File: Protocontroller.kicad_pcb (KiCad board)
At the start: 4 copper layers, 51 x 26.4 mm, 39 parts, among them U1 AP2112K-3.3TRG1, U2 PM254-1-14-Z-8.5, U3 PM254-1-14-Z-8.5, U4 SN74AHCT245PWR, U5 SN74AHCT245PWR, U6 SN74AHCT374PWR, U8 HC-JN254-2-08-W

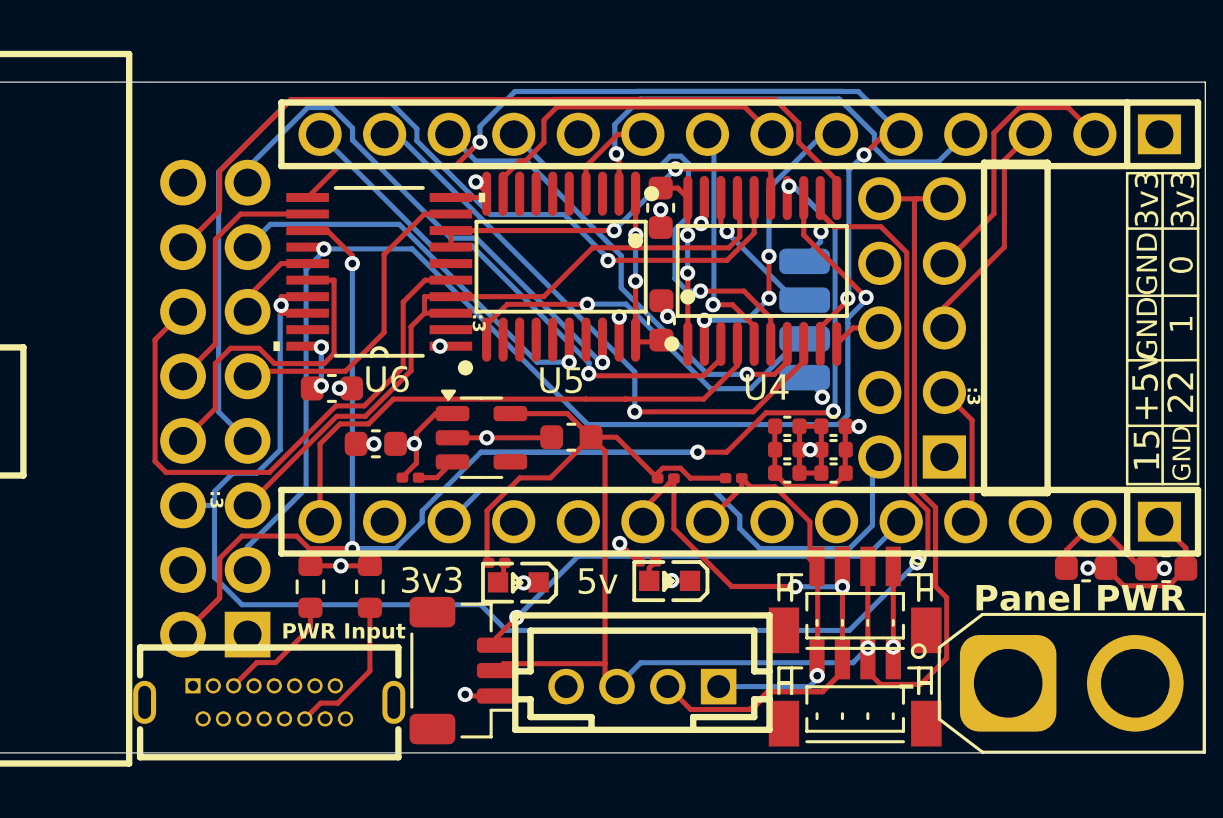
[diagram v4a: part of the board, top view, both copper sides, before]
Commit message: Switch Pullups to use 4.7k Resistors for improved speeds, Adjusted capacitors, removed Designators file
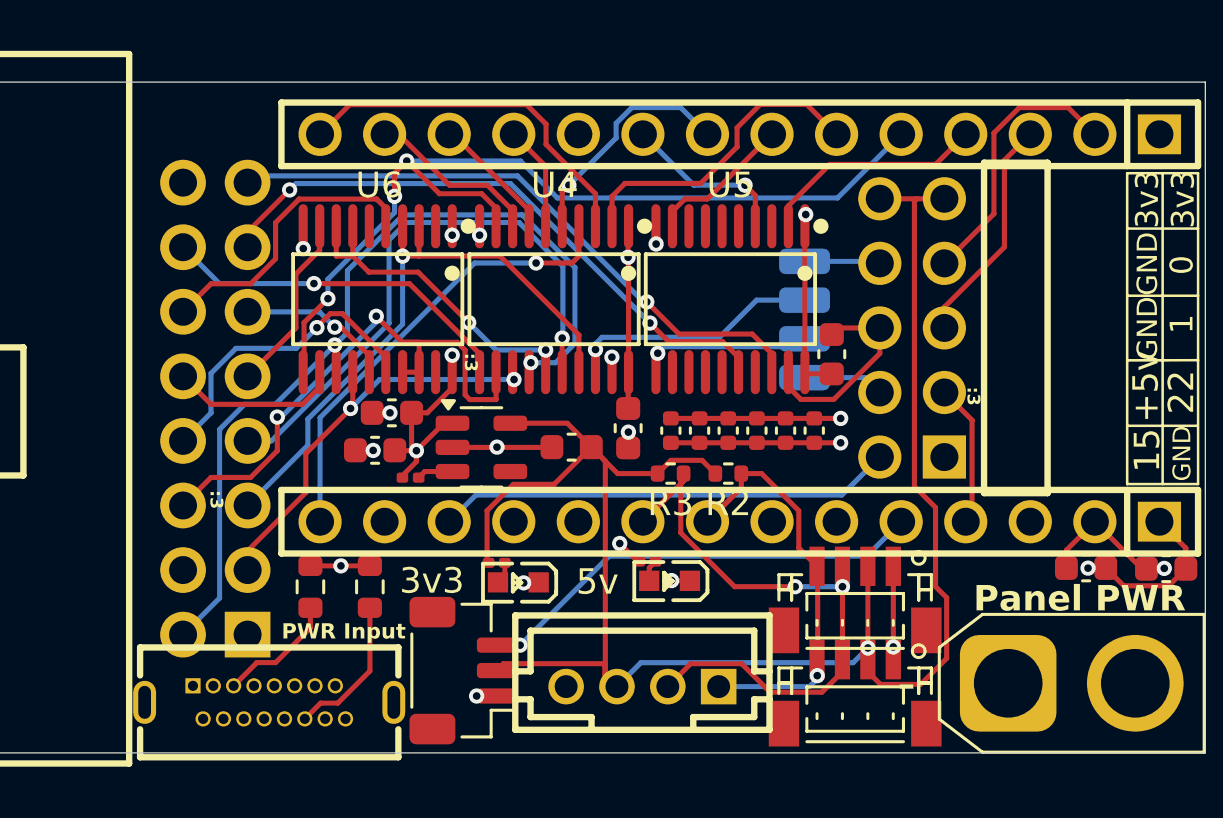
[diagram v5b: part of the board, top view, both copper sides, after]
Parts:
- R2, R3: value 10K_0201 -> 4.7K_0402; footprint Resistor_SMD:R_0201_0603Metric -> Resistor_SMD:R_0402_1005Metric
- moved C6 8.76 mm to (116.3, 126.1)
- moved U4 8.27 mm to (113.3, 121.0), turned to 180 degrees
- moved C5 6.83 mm to (124.3, 123.2)
- moved U5 6.78 mm to (120.3, 121.0)
- moved C8 6.61 mm to (117.9, 126.2), turned to -90 degrees
- moved C9 3.83 mm to (119.1, 126.2), turned to -90 degrees
- moved C7 2.55 mm to (107.0, 125.5), turned to 0 degrees
- moved C10 2.44 mm to (120.2, 126.2), turned to -90 degrees
- moved C12 2.03 mm to (122.5, 126.2), turned to -90 degrees
- moved C11 1.21 mm to (121.3, 126.2), turned to -90 degrees
- moved U6 1.08 mm to (106.4, 121.0)
- moved C13 0.78 mm to (123.6, 126.2), turned to -90 degrees
- moved C2 0.39 mm to (114.0, 126.9)
- moved U1 0.38 mm to (110.5, 126.9)
- moved R2 0.28 mm to (120.2, 127.9)
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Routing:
- net /PANEL_G2: track 64.9 -> 22.5 mm
- net /PANEL_G1: track 69.3 -> 34.9 mm, vias 5 -> 2
- net /PANEL_B1: track 48.0 -> 16.7 mm
- net /PANEL_LATCH: track 31.5 -> 14.1 mm, vias 0 -> 1
- net /BUFFER_G2/MOSI: track 23.9 -> 6.90 mm, vias 1 -> 0
- net /PANEL_B2: track 38.1 -> 22.8 mm
- net /BUFFER_B1: track 19.0 -> 5.01 mm, vias 1 -> 0
- net /BUFFER_G1: track 17.9 -> 4.14 mm, vias 1 -> 0
- net /PANEL_ADX3: track 22.8 -> 11.5 mm
- net /BUFFER_OE: track 18.8 -> 8.95 mm, vias 1 -> 0
- net /APA_DAT: track 15.6 -> 6.78 mm
- net /PANEL_CLK: track 16.2 -> 24.1 mm, vias 1 -> 2
- net /FLEXIO_MOSI: track 13.3 -> 5.75 mm
- net GND: track 45.7 -> 52.2 mm, vias 17 -> 16
- net /BUFFER_R2: track 20.8 -> 14.5 mm, vias 1 -> 0
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
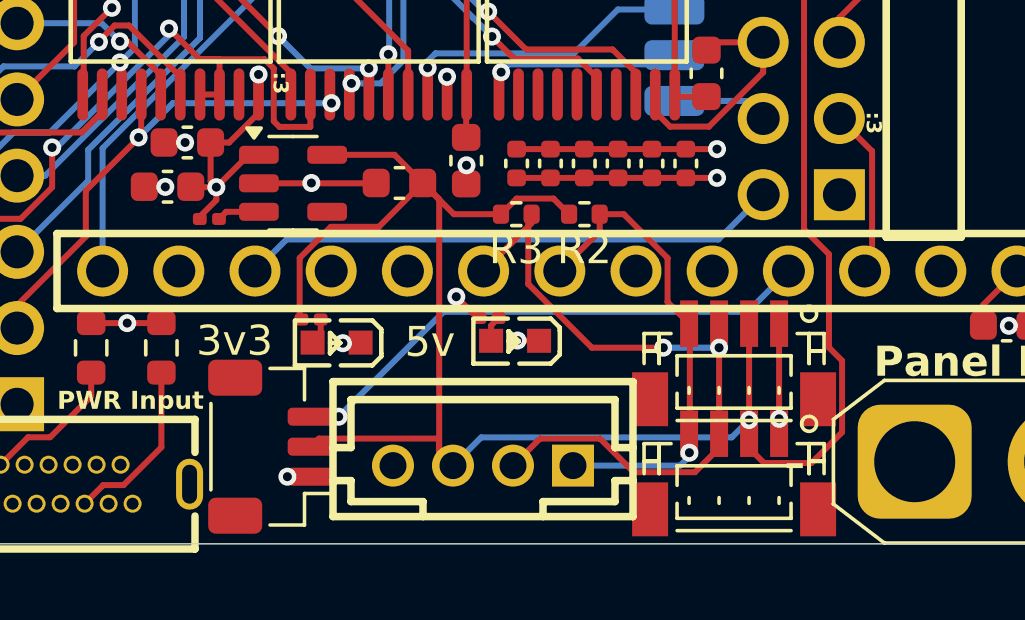
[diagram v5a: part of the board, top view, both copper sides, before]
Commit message: Removed 0201 Resistors for Compatablity with Economic PCBA's, moved JST SH ports so I2C-1 Pins dont phase through teensy headers
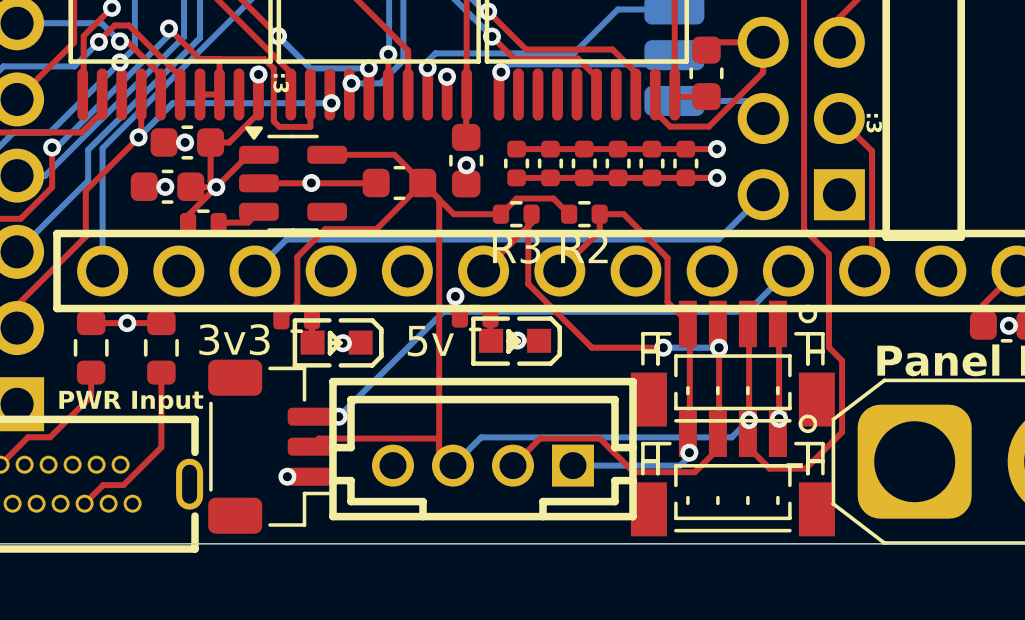
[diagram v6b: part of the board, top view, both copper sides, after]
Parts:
- R1, R4, R5: footprint Resistor_SMD:R_0201_0603Metric -> Resistor_SMD:R_0402_1005Metric
- moved R4 0.48 mm to (110.6, 131.4)
- moved R5 0.46 mm to (116.6, 131.4)
- moved R1 0.23 mm to (107.5, 128.2)

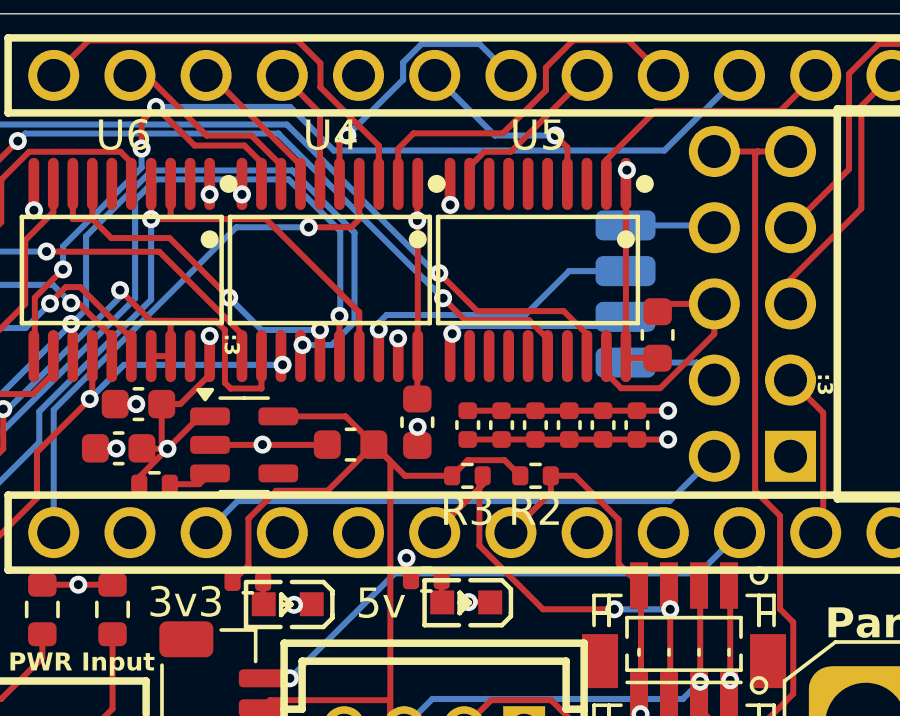
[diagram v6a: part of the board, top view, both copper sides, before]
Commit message: Fix Compat with Economic Again
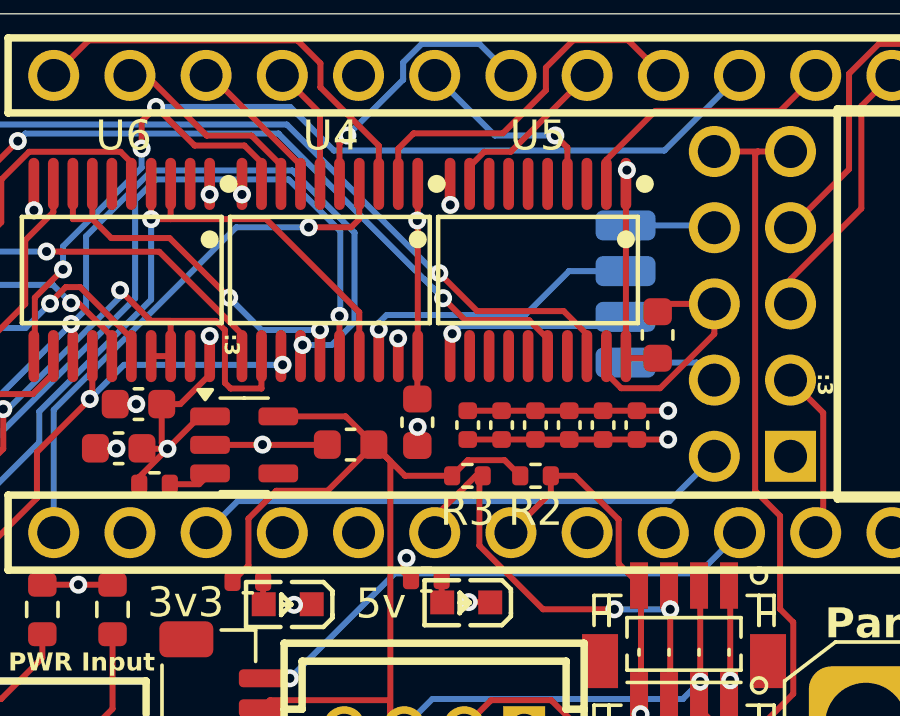
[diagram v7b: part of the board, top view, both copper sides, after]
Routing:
- net +5V: track 54.6 -> 53.9 mm
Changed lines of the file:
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@@
-	)
-	(segment
-		(start 116.258 119.39)
-		(end 116.258 118.765)
-		(width 0.2)
-		(layer "F.Cu")
-		(net 1)
 	)
 	(segment
@@
 	)
 	(segment
+		(start 116.275 119.373)
+		(end 116.258 119.39)
+		(width 0.2)
+		(layer "F.Cu")
+		(net 1)
+	)
+	(segment
 		(start 109.3375 123.91)
 		(end 109.3375 124.5325)
@@
 	)
 	(segment
-		(start 116.258 118.765)
-		(end 116.275 118.748)
-		(width 0.2)
-		(layer "F.Cu")
-		(net 1)
-	)
-	(segment
 		(start 138.2 131.64)
 		(end 137.524 132.316)
@@
 	)
 	(segment
+		(start 116.275 118.17)
+		(end 116.275 119.373)
+		(width 0.2)
+		(layer "F.Cu")
+		(net 1)
+	)
+	(segment
 		(start 107.74 125.51)
 		(end 107.74 126.809)
@@
 	)
 	(segment
-		(start 116.258 118.765)
-		(end 116.258 118.14)
-		(width 0.2)
-		(layer "F.Cu")
-		(net 1)
-	)
-	(segment
 		(start 115.79 130.75)
 		(end 115.79 131.1)
@@
 	)
 	(segment
-		(start 116.275 118.748)
-		(end 116.275 118.17)
-		(width 0.2)
-		(layer "F.Cu")
-		(net 1)
-	)
-	(segment
 		(start 123.212 117.9965)
 		(end 123.212 117.743)
@@
 	)
 	(segment
+		(start 118.21 127.9)
+		(end 118.44 127.9)
+		(width 0.2)
+		(layer "F.Cu")
+		(net 14)
+	)
+	(segment
+		(start 118.329 128.011)
+		(end 118.329 130.229339)
+		(width 0.2)
+		(layer "F.Cu")
+		(net 14)
+	)
+	(segment
+		(start 117.689 128.421)
+		(end 117.697918 128.421)
+		(width 0.2)
+		(layer "F.Cu")
+		(net 14)
+	)
+	(segment
 		(start 121.842 136.5)
 		(end 120.721 135.379)
@@
 	)
 	(segment
+		(start 124.69 132.35)
+		(end 124.69 135.2175)
+		(width 0.2)
+		(layer "F.Cu")
+		(net 14)
+	)
+	(segment
+		(start 117.891 128.227918)
+		(end 117.891 128.219)
+		(width 0.2)
+		(layer "F.Cu")
+		(net 14)
+	)
+	(segment
+		(start 124.69 135.2175)
+		(end 124.69 135.6945)
+		(width 0.2)
+		(layer "F.Cu")
+		(net 14)
+	)
+	(segment
+		(start 116.84 129.794)
+		(end 116.84 129.27)
+		(width 0.2)
+		(layer "F.Cu")
+		(net 14)
+	)
+	(segment
+		(start 118.44 127.9)
+		(end 118.329 128.011)
+		(width 0.2)
+		(layer "F.Cu")
+		(net 14)
+	)
+	(segment
+		(start 118.721 135.379)
+		(end 117.82 136.28)
+		(width 0.2)
+		(layer "F.Cu")
+		(net 14)
+	)
+	(segment
+		(start 118.329 130.229339)
+		(end 120.449661 132.35)
+		(width 0.2)
+		(layer "F.Cu")
+		(net 14)
+	)
+	(segment
+		(start 117.891 128.219)
+		(end 118.21 127.9)
+		(width 0.2)
+		(layer "F.Cu")
+		(net 14)
+	)
+	(segment
+		(start 120.721 135.379)
+		(end 118.721 135.379)
+		(width 0.2)
+		(layer "F.Cu")
+		(net 14)
+	)
+	(segment
+		(start 123.8845 136.5)
+		(end 121.842 136.5)
+		(width 0.2)
+		(layer "F.Cu")
+		(net 14)
+	)
+	(segment
+		(start 124.69 131.548)
+		(end 124.69 132.35)
+		(width 0.2)
+		(layer "F.Cu")
+		(net 14)
+	)
+	(segment
 		(start 120.449661 132.35)
 		(end 122.83 132.35)
@@
 	)
 	(segment
-		(start 124.69 132.35)
-		(end 124.69 135.2175)
-		(width 0.2)
-		(layer "F.Cu")
-		(net 14)
-	)
-	(segment
-		(start 118.329 130.229339)
-		(end 120.449661 132.35)
-		(width 0.2)
-		(layer "F.Cu")
-		(net 14)
-	)
-	(segment
-		(start 124.69 135.2175)
-		(end 124.69 135.6945)
-		(width 0.2)
-		(layer "F.Cu")
-		(net 14)
-	)
-	(segment
-		(start 118.44 127.9)
-		(end 118.329 128.011)
-		(width 0.2)
-		(layer "F.Cu")
-		(net 14)
-	)
-	(segment
-		(start 118.721 135.379)
-		(end 117.82 136.28)
-		(width 0.2)
-		(layer "F.Cu")
-		(net 14)
-	)
-	(segment
-		(start 120.721 135.379)
-		(end 118.721 135.379)
-		(width 0.2)
-		(layer "F.Cu")
-		(net 14)
-	)
-	(segment
-		(start 123.8845 136.5)
-		(end 121.842 136.5)
-		(width 0.2)
-		(layer "F.Cu")
-		(net 14)
-	)
-	(segment
-		(start 124.69 131.548)
-		(end 124.69 132.35)
-		(width 0.2)
-		(layer "F.Cu")
-		(net 14)
-	)
-	(segment
-		(start 116.84 129.794)
-		(end 118.44 128.194)
-		(width 0.2)
-		(layer "F.Cu")
-		(net 14)
-	)
-	(segment
 		(start 124.69 131.5475)
 		(end 124.69 131.548)
@@
 	)
 	(segment
-		(start 118.329 128.011)
-		(end 118.329 130.229339)
-		(width 0.2)
-		(layer "F.Cu")
-		(net 14)
-	)
-	(segment
-		(start 118.44 128.194)
-		(end 118.44 127.9)
-		(width 0.2)
-		(layer "F.Cu")
+		(start 116.84 129.27)
+		(end 117.689 128.421)
+		(width 0.2)
+		(layer "F.Cu")
+		(net 14)
+	)
+	(segment
+		(start 117.697918 128.421)
+		(end 117.891 128.227918)
+		(width 0.2)
+		(layer "F.Cu")

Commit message: Fix Economic Again, fix R1 not being connected, V2 tba
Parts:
- removed Logo: LOGO, LOGO
- removed PWR-Input1: TYPE-C 16PFS LCH7.45 IPX8, Protocontroller:USB-TH_TYPE-C-16PFS-LCH7.45-IPX8
- added LOGO: LOGO, LOGO, B.Cu at (123.7, 40.0)
- added PWR-Input: TYPE-C 16PFS LCH7.45 IPX8, Protocontroller:USB-C-TH_TYPE-C-6PLCH10.0-073, F.Cu at (91.5, 55.1)
- R2: value 4.7K_0402 -> 4.7K_402
- U4, U5: value SN74AHCT245PWR -> 74245PW
- U6: value SN74AHCT374PWR -> 74374PW
- moved R6 83.0 mm to (93.2, 50.3)
- moved Mic 82.7 mm to (98.9, 53.6)
- moved C7 82.7 mm to (96.3, 43.5)
- moved 3v3 82.7 mm to (101.3, 50.2)
- moved 5v 82.7 mm to (107.3, 50.1)
- moved C1 82.7 mm to (95.7, 45.0)
- moved C2 82.7 mm to (103.4, 44.8)
- moved C3 82.7 mm to (123.7, 49.6)
- moved C5 82.7 mm to (113.7, 41.2)
- moved C6 82.7 mm to (105.7, 44.1)
- moved I2C-3 82.7 mm to (106.2, 54.3)
- moved IO1 82.7 mm to (116.8, 40.2)
- moved Panel-PWR 82.7 mm to (120.6, 54.1)
- moved QR 82.7 mm to (80.7, 53.5)
- moved R1 82.7 mm to (96.9, 46.2)
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- renumbered Panel-PWR1 to Panel-PWR
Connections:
- IO1 pad 5: /DIGITAL2 -> /DIGITAL1
- IO1 pad 7: /DIGITAL1 -> GND
- IO1 pad 8: GND -> /DIGITAL2
- U4 pad 15: Net-(U4-B4) -> /PANEL_R1
- U6 pad 7: Net-(U4-B4) -> /PANEL_R1
- U6 pad 8: Net-(U4-B4) -> /PANEL_R1
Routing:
- net /PANEL_R1: track 0.00 -> 30.4 mm, vias 0 -> 1
- net Net-(U4-B4): track 13.0 -> 0.00 mm, vias 2 -> 0
- net GND: track 52.2 -> 46.9 mm
- net +5V: track 53.9 -> 58.0 mm
- net /PANEL_G1: track 34.9 -> 37.3 mm
- net +3.3V: track 72.5 -> 73.8 mm
- net /PANEL_G2: track 22.5 -> 21.3 mm
- net Net-(PWR-Input1-CC2): track 5.83 -> 4.71 mm
- net /PANEL_B1: track 16.7 -> 17.3 mm
- net /BUFFER_LATCH: track 36.1 -> 36.6 mm
- net /PANEL_CLK: track 24.1 -> 24.5 mm, vias 2 -> 1
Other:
- board text removed: "PWR Input"
- board text removed: "Panel PWR"
